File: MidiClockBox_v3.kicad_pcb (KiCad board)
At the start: 2 copper layers, 219 x 100 mm, 89 parts, among them J1 Midi In 0, J10 Display, J11 Midi Out 3, J12 Midi Out 4, J13 Midi Out 5, J14 Sync Out 0, J15 Sync Out 1, J16 Spare, J17 Conn_01x07, J18 Conn_01x07, J19 Conn_02x05_Odd_Even, J2 ICSP, J20 Conn_02x05_Odd_Even, J3 WS2812, J4 Conn_02x07_Odd_Even, J5 Conn_02x12_Counter_Clockwise, J6 Midi Out 0, J7 Midi Out 1, J8 Midi Out 2, J9 WS2812, SW1 RotaryEncoder_Switch, SW2 TAP, SW3 Start, SW4 Stop, SW5 Preset1, SW6 Preset2, SW7 Preset3, U1 CD74HC4067SM, U2 74LS241, U3 6N138, U4 74HC595, U6 74LS08, U7 74LS08, U8 74HC595, U9 74LS241

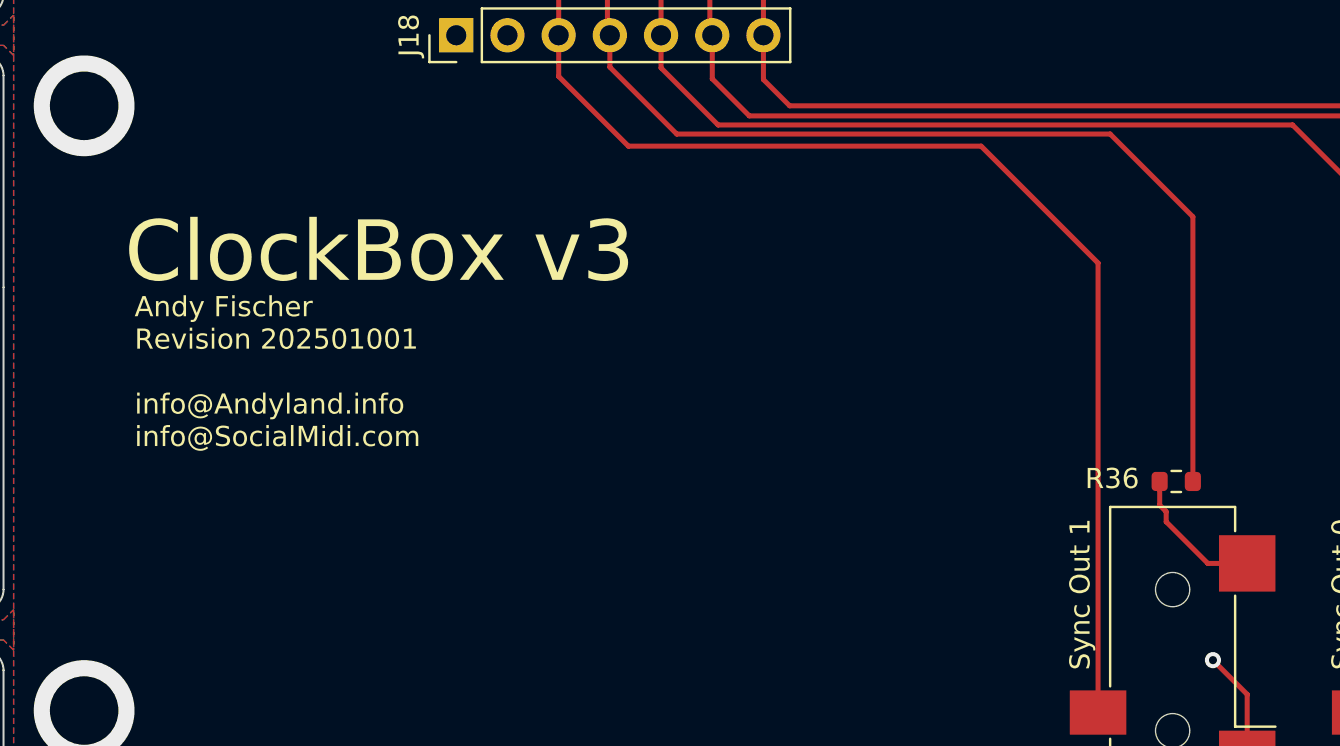
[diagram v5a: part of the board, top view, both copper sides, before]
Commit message: change silkscreen info's size
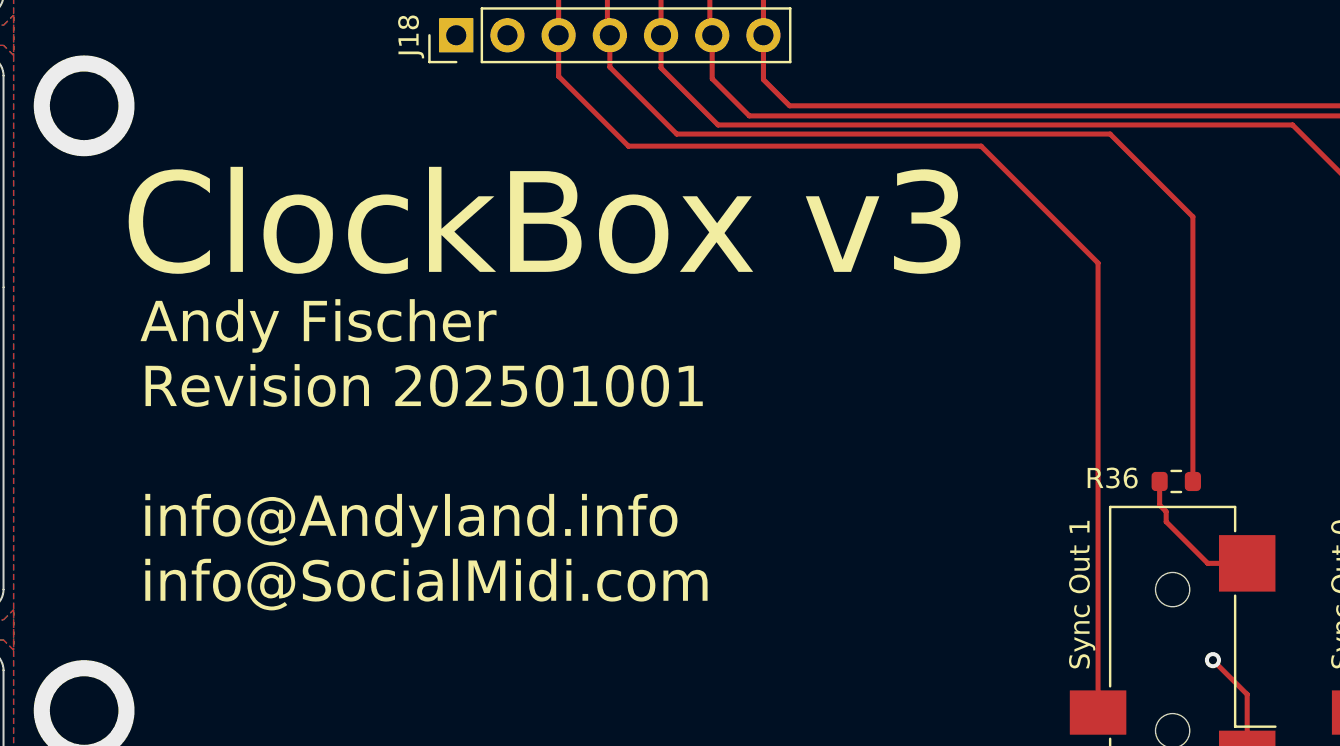
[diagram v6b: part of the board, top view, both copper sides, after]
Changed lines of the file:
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@@
 	)
 	(gr_text "Andy Fischer\nRevision 202501001\n\ninfo@Andyland.info\ninfo@SocialMidi.com"
-		(at 150.5 104 0)
+		(at 150.775 111.8 0)
 		(layer "F.SilkS")
 		(effects
 			(font
-				(size 1 1)
-				(thickness 0.15)
+				(size 2 2)
+				(thickness 0.3)
 			)
 			(justify left bottom)
@@
 	)
 	(gr_text "ClockBox v3"
-		(at 150 96 0)
+		(at 149.825 95.85 0)
 		(layer "F.SilkS")
 		(effects
 			(font
-				(size 3 3)
-				(thickness 0.45)
+				(size 5 5)
+				(thickness 0.75)
 			)
 			(justify left bottom)

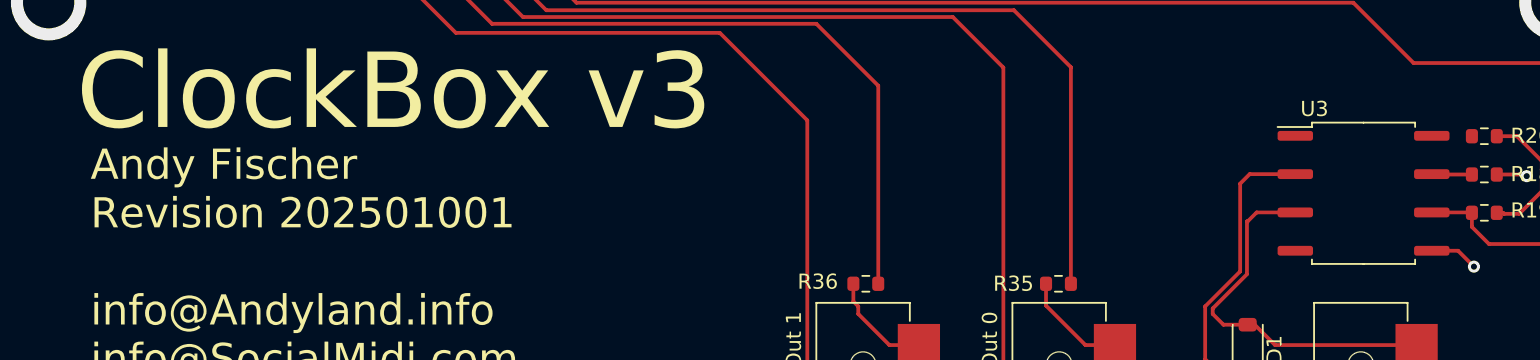
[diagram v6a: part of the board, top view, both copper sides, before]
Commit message: fix Adafruit LED pinout and BOM
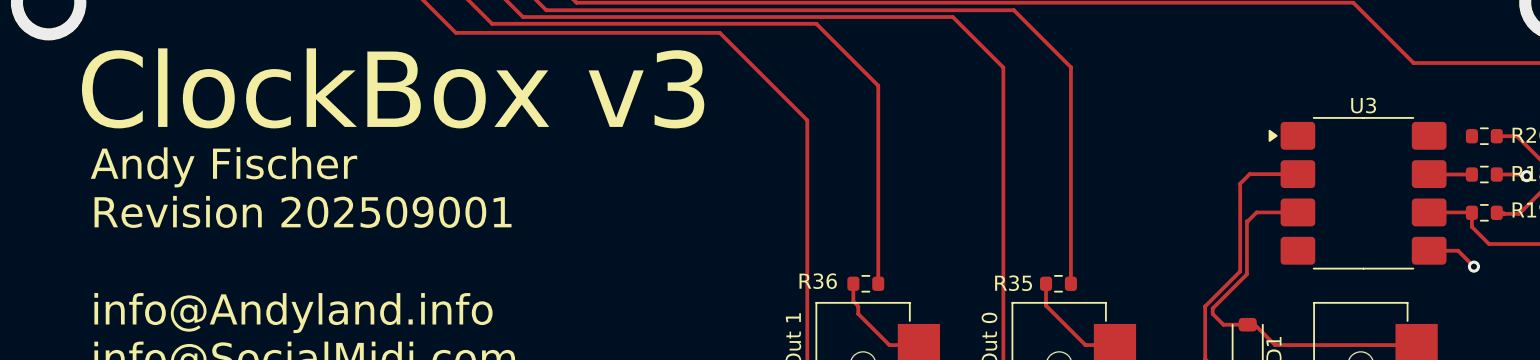
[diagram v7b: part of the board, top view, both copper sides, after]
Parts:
- U3: footprint Package_SO:SOP-8_6.62x9.15mm_P2.54mm -> Package_SO:SOP-8_6.605x9.655mm_P2.54mm
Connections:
- D2 pad 1: +5V -> GND
- D2 pad 2: Net-(D2-DOUT) -> LED_DATA
- D2 pad 3: GND -> +5V
- D2 pad 4: LED_DATA -> Net-(D2-DOUT)
- D3 pad 1: +5V -> GND
- D3 pad 2: Net-(D3-DOUT) -> Net-(D2-DOUT)
- D3 pad 3: GND -> +5V
- D3 pad 4: Net-(D2-DOUT) -> Net-(D3-DIN)
- D4 pad 1: +5V -> GND
- D4 pad 2: Net-(D4-DOUT) -> Net-(D3-DIN)
- D4 pad 3: GND -> +5V
- D4 pad 4: Net-(D3-DOUT) -> Net-(D4-DIN)
- D5 pad 1: +5V -> GND
- D5 pad 2: Net-(D5-DOUT) -> Net-(D4-DIN)
- D5 pad 3: GND -> +5V
- D5 pad 4: Net-(D4-DOUT) -> Net-(D5-DIN)
- D6 pad 1: +5V -> GND
- D6 pad 2: unconnected-(D6-DOUT-Pad2) -> Net-(D5-DIN)
- D6 pad 3: GND -> +5V
- D6 pad 4: Net-(D5-DOUT) -> unconnected-(D6-DOUT-Pad4)
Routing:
- net Net-(D5-DOUT): track 23.7 -> 0.00 mm
- net Net-(D5-DIN): track 0.00 -> 23.7 mm
- net Net-(D4-DOUT): track 14.9 -> 0.00 mm
- net Net-(D4-DIN): track 0.00 -> 14.9 mm
- net Net-(D3-DOUT): track 13.8 -> 0.00 mm
- net Net-(D3-DIN): track 0.00 -> 13.8 mm
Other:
- board text added: "Andy Fischer Revision 202509001 info@Andyland.info info@SocialMidi.com"
- board text removed: "Andy Fischer Revision 202501001 info@Andyland.info info@SocialMidi.com"

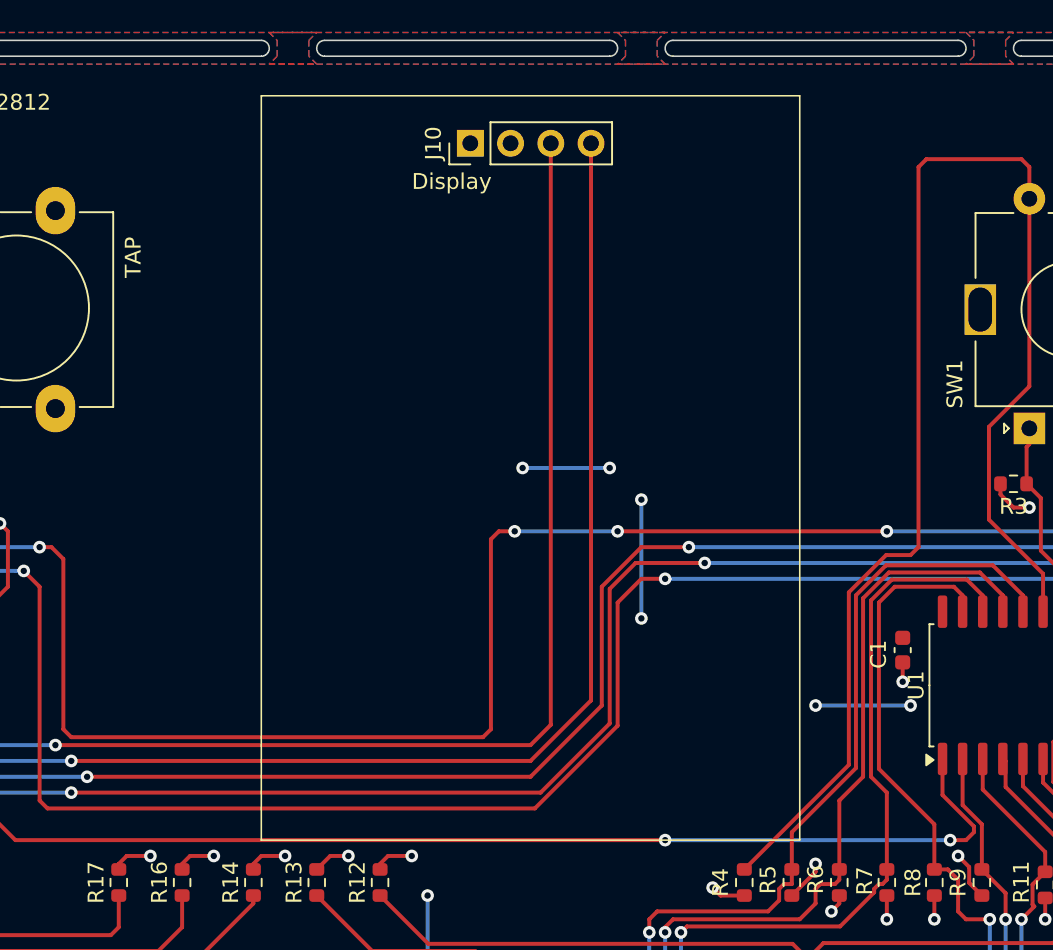
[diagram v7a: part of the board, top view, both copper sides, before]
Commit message: add title and revision to schema and pcb
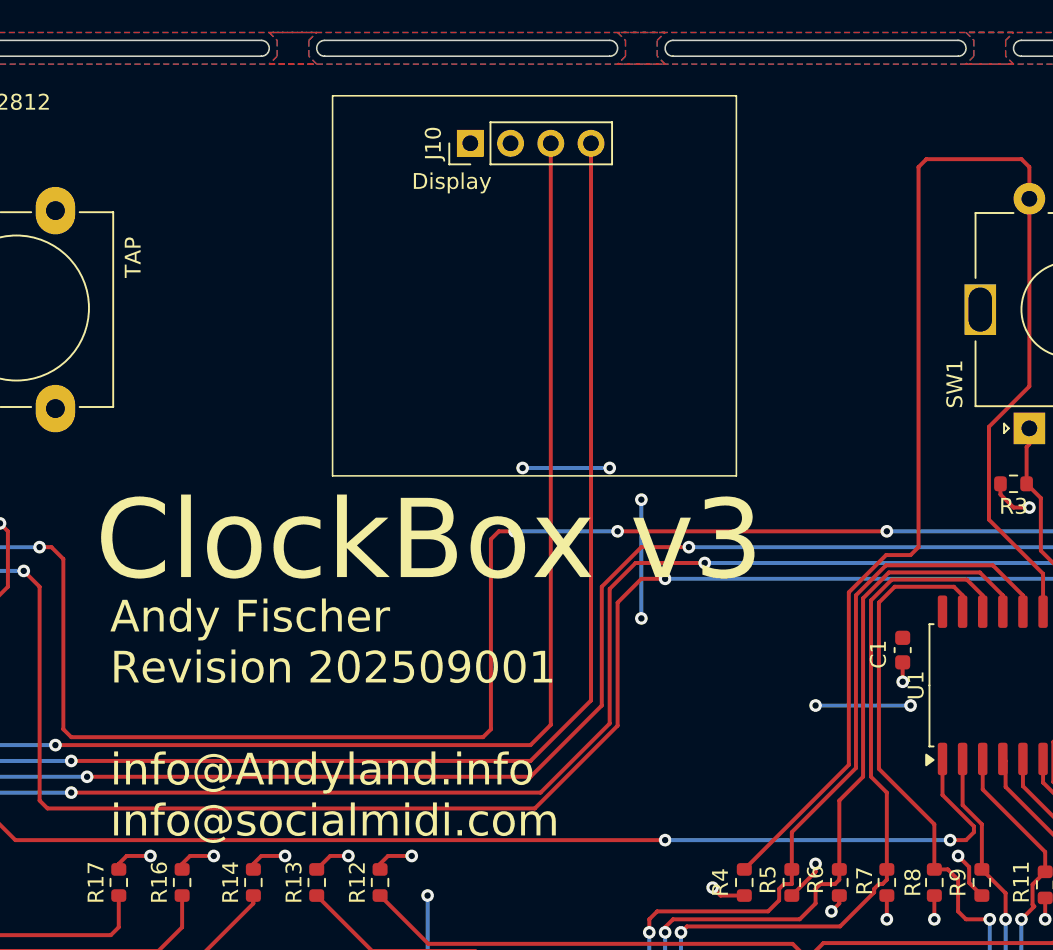
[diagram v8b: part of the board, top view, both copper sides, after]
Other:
- board text added: "Andy Fischer Revision 202509001 info@Andyland.info info@socialmidi.com"
